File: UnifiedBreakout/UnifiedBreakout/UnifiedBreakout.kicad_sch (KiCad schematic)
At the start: 39 parts, among them J1 24V DC IN, J2 ATX-24, J22 DRAWBAR, J23 MIST, J24 AXIS PWR IN, J25 AXIS PWR OUT, J3 5V BUS, J4 24V BUS, J5 12V BUS, U1 4N35, U7 74HC14

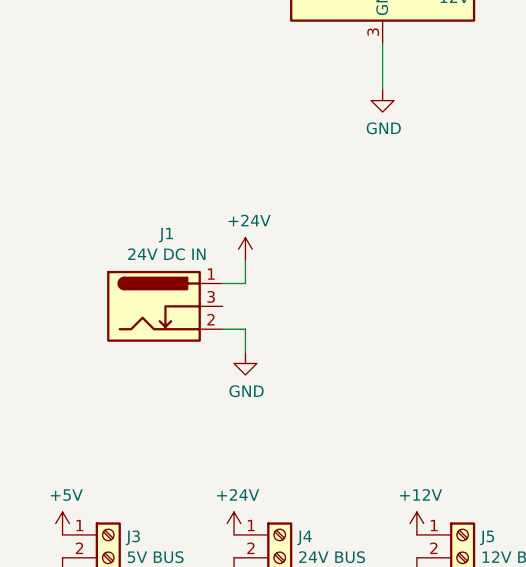
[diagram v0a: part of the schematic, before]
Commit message: Upgrade to new KiCAD version
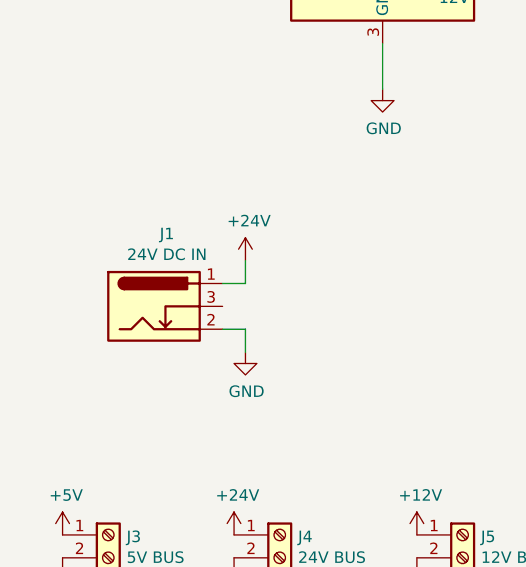
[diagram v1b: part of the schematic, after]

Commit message: WIP updating breakout for electrical enclosure
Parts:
- removed C1, C5: 100n, Capacitor_THT:C_Disc_D5.0mm_W2.5mm_P5.00mm, symbol UnifiedBreakout-rescue:C-Device
- removed C2, C6: 100uF, Capacitor_THT:CP_Radial_D8.0mm_P3.50mm, symbol UnifiedBreakout-rescue:CP-Device
- removed D3: ATX PWR GOOD, LED_THT:LED_D3.0mm, symbol UnifiedBreakout-rescue:LED-Device
- removed D4: ATX STBY, LED_THT:LED_D3.0mm, symbol UnifiedBreakout-rescue:LED-Device
- removed J1: 24V DC IN, SwitchCraft-BarrelJack-RAPC722BK:RAPC722BK, symbol UnifiedBreakout-rescue:Barrel_Jack_Switch-Connector
- removed J2: ATX-24, Connector_Molex:Molex_Mini-Fit_Jr_5569-24A2_2x12_P4.20mm_Horizontal, symbol UnifiedBreakout-rescue:ATX-24-Connector
- removed J22: DRAWBAR, Connector_Phoenix_MSTB:PhoenixContact_MSTBA_2,5_2-G-5,08_1x02_P5.08mm_Horizontal, symbol UnifiedBreakout-rescue:Screw_Terminal_01x02-Connector
- removed J23: MIST, Connector_Phoenix_MSTB:PhoenixContact_MSTBA_2,5_2-G-5,08_1x02_P5.08mm_Horizontal, symbol UnifiedBreakout-rescue:Screw_Terminal_01x02-Connector
- removed J3: 5V BUS, Connector_Phoenix_MSTB:PhoenixContact_MSTBA_2,5_2-G-5,08_1x02_P5.08mm_Horizontal, symbol UnifiedBreakout-rescue:Screw_Terminal_01x02-Connector
- removed J5: 12V BUS, Connector_Phoenix_MSTB:PhoenixContact_MSTBA_2,5_2-G-5,08_1x02_P5.08mm_Horizontal, symbol UnifiedBreakout-rescue:Screw_Terminal_01x02-Connector
- removed R1: 2K2, Resistor_THT:R_Axial_DIN0207_L6.3mm_D2.5mm_P7.62mm_Horizontal, symbol UnifiedBreakout-rescue:R-Device
- removed R25: 10K, Resistor_THT:R_Axial_DIN0207_L6.3mm_D2.5mm_P7.62mm_Horizontal, symbol UnifiedBreakout-rescue:R-Device
- removed R4, R5: 220R, Resistor_THT:R_Axial_DIN0207_L6.3mm_D2.5mm_P7.62mm_Horizontal, symbol UnifiedBreakout-rescue:R-Device
- removed unit 2 of U7
- added J1: DRAWBAR+MIST, Connector_Phoenix_MSTB:PhoenixContact_MSTBA_2,5_2-G-5,08_1x02_P5.08mm_Horizontal, symbol Connector:Screw_Terminal_01x02
- added J2: Screw_Terminal_01x05, Connector_Phoenix_MSTB:PhoenixContact_MSTBA_2,5_5-G-5,08_1x05_P5.08mm_Horizontal, symbol Connector:Screw_Terminal_01x06
- added Q2, Q4: 2N7000, Package_TO_SOT_THT:TO-92_Inline, symbol Transistor_FET:2N7000
- added R1: 10K, Resistor_THT:R_Axial_DIN0207_L6.3mm_D2.5mm_P7.62mm_Horizontal, symbol Device:R
- added unit 6 of U7
- added unit 5 of U7
- added unit 4 of U7
- added unit 2 of U7
- C3, C7: symbol UnifiedBreakout-rescue:C-Device -> Device:C
- C4, C8: symbol UnifiedBreakout-rescue:CP-Device -> Device:C_Polarized
- D1, D2: symbol UnifiedBreakout-rescue:LED-Device -> Device:LED
- H1, H2, H3, H4, H5, H6: symbol UnifiedBreakout-rescue:MountingHole-Mechanical -> Mechanical:MountingHole
- J24, J25: symbol UnifiedBreakout-rescue:Screw_Terminal_01x03-Connector -> Connector:Screw_Terminal_01x03; Farnell PN (none) -> 3041451; MPN 1757255 -> 1729131
- J4: symbol UnifiedBreakout-rescue:Screw_Terminal_01x02-Connector -> Connector:Screw_Terminal_01x02; MPN 1757242 -> (none); Manufacturer Phoenix Contact -> My parts drawers
- R2, R24, R26, R3, R6, R7: symbol UnifiedBreakout-rescue:R-Device -> Device:R
- U1: symbol UnifiedBreakout-rescue:4N35-Isolator -> Isolator:4N35
- U7: symbol UnifiedBreakout-rescue:74HC14-74xx -> 74xx:74HC14
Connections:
- net +5VP: now also R1.1
- net DRAWBAR_VALVE: now also R1.2, U7.3
- net GND: now also Q2.1 (S), Q4.1 (S)
- net MIST RELAY/ENABLE: no longer names the net of U7.6
- net MIST RELAY/ENABLE: now also Q4.2 (G)
- new net: Q2.2 (G), U7.4
- new net: J1.1 (Pin_1), Q2.3 (D)
- new net: J1.2 (Pin_2), Q4.3 (D)
- new net DRAWBAR SW/INPUT: J2.6 (Pin_6)
- new net LIM X/INPUT: J2.1 (Pin_1)
- new net LIM Y/INPUT: J2.2 (Pin_2)
- new net LIM Z/INPUT: J2.3 (Pin_3)
- new net PROBE/INPUT: J2.4 (Pin_4)
- new net TOOL_PROBE/INPUT: J2.5 (Pin_5)
- no-connect marks 0 -> 12
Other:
- removed sheet DRAWBAR RELAY
- removed sheet MIST RELAY
- added sheet TOOL_PROBE (opto_input.kicad_sch)
- sheet ARGON ENCODER ports: added none; removed MESA_5V
- sheet ARGON ESTOP ports: added GND; removed Gnd
- sheet AXIS POWER RELAY ports: added +24V; removed +12V
- sheet DRAWBAR SW ports: added INPUT; removed 24V, 5V
- sheet LIM X ports: added INPUT; removed 24V, 5V
- sheet LIM Y ports: added INPUT; removed 24V, 5V
- sheet LIM Z ports: added INPUT; removed 24V, 5V
- sheet PROBE ports: added INPUT; removed 24V, 5V
- moved on the sheet: R26, U7C

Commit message: Add stacked DA15 part
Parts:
- J2: footprint Connector_Phoenix_MSTB:PhoenixContact_MSTBA_2,5_5-G-5,08_1x05_P5.08mm_Horizontal -> Connector_Phoenix_MSTB:PhoenixContact_MSTBA_2,5_6-G-5,08_1x06_P5.08mm_Horizontal; Farnell PN 3041487 -> 3041499; MPN 1729157 -> 1729160
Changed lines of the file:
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@@
       (effects (font (size 1.27 1.27)) (justify left))
     )
-    (property "Footprint" "Connector_Phoenix_MSTB:PhoenixContact_MSTBA_2,5_5-G-5,08_1x05_P5.08mm_Horizontal" (at 325.12 78.74 0)
+    (property "Footprint" "Connector_Phoenix_MSTB:PhoenixContact_MSTBA_2,5_6-G-5,08_1x06_P5.08mm_Horizontal" (at 325.12 78.74 0)
       (effects (font (size 1.27 1.27)) hide)
     )
@@
       (effects (font (size 1.27 1.27)) hide)
     )
-    (property "Farnell PN" "3041487" (at 325.12 78.74 0)
+    (property "Farnell PN" "3041499" (at 325.12 78.74 0)
       (effects (font (size 1.27 1.27)) hide)
     )
-    (property "MPN" "1729157 " (at 325.12 78.74 0)
+    (property "MPN" "1729160" (at 325.12 78.74 0)
       (effects (font (size 1.27 1.27)) hide)
     )

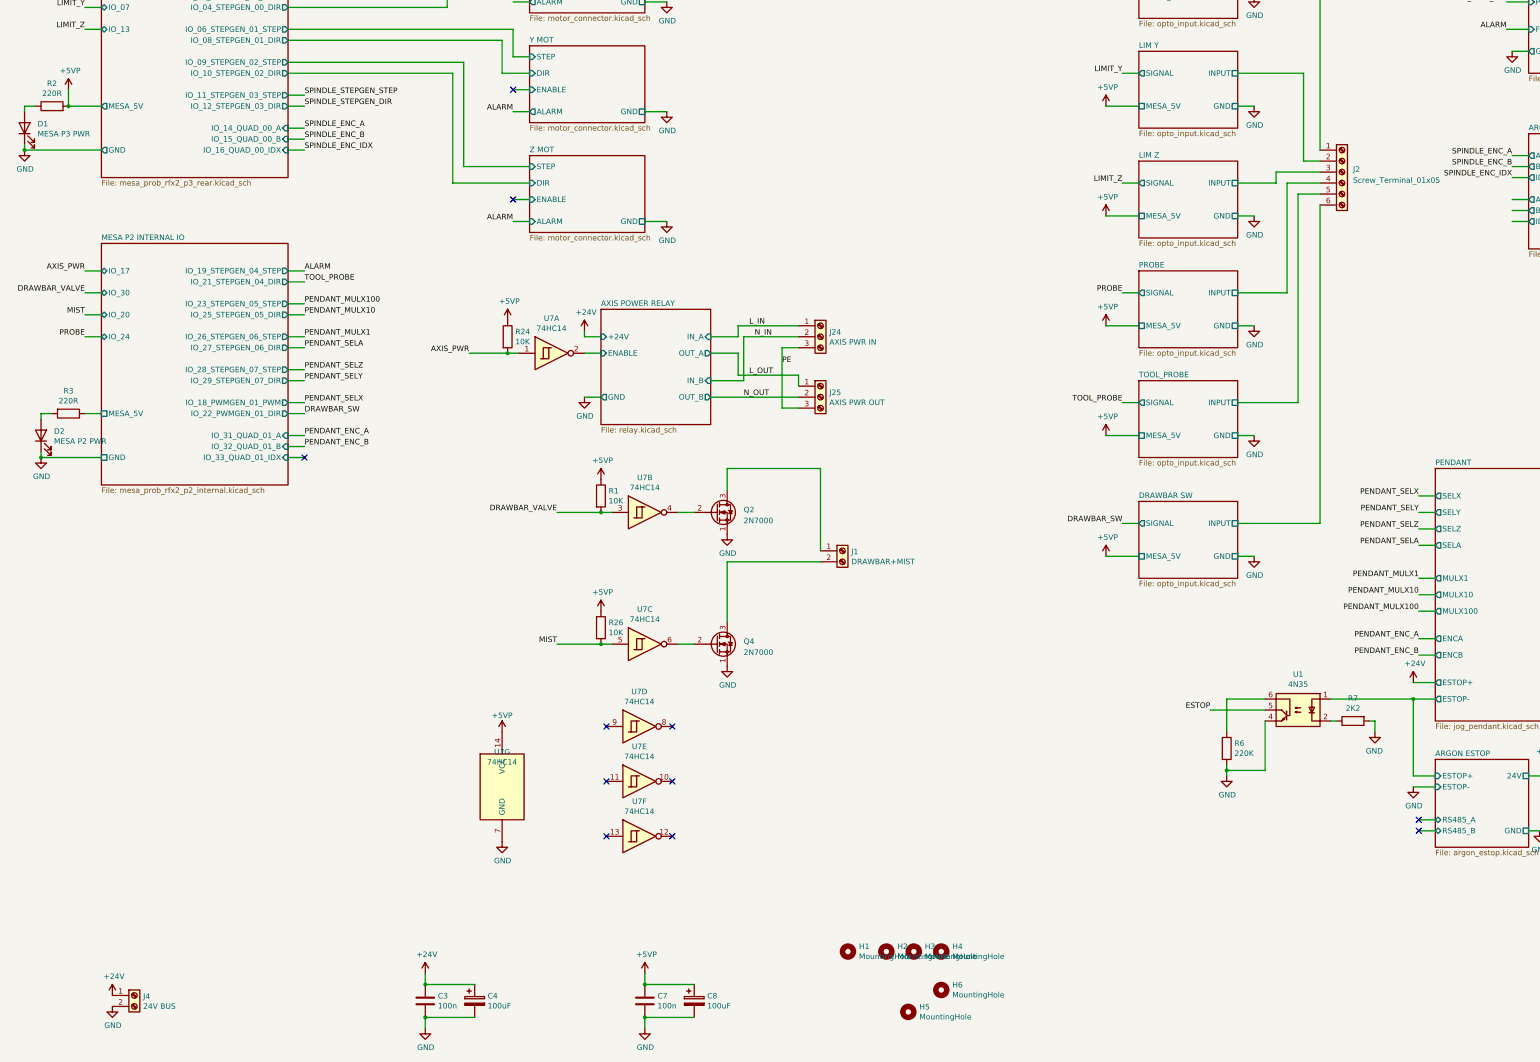
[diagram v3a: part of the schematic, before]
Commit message: Update IO and opto
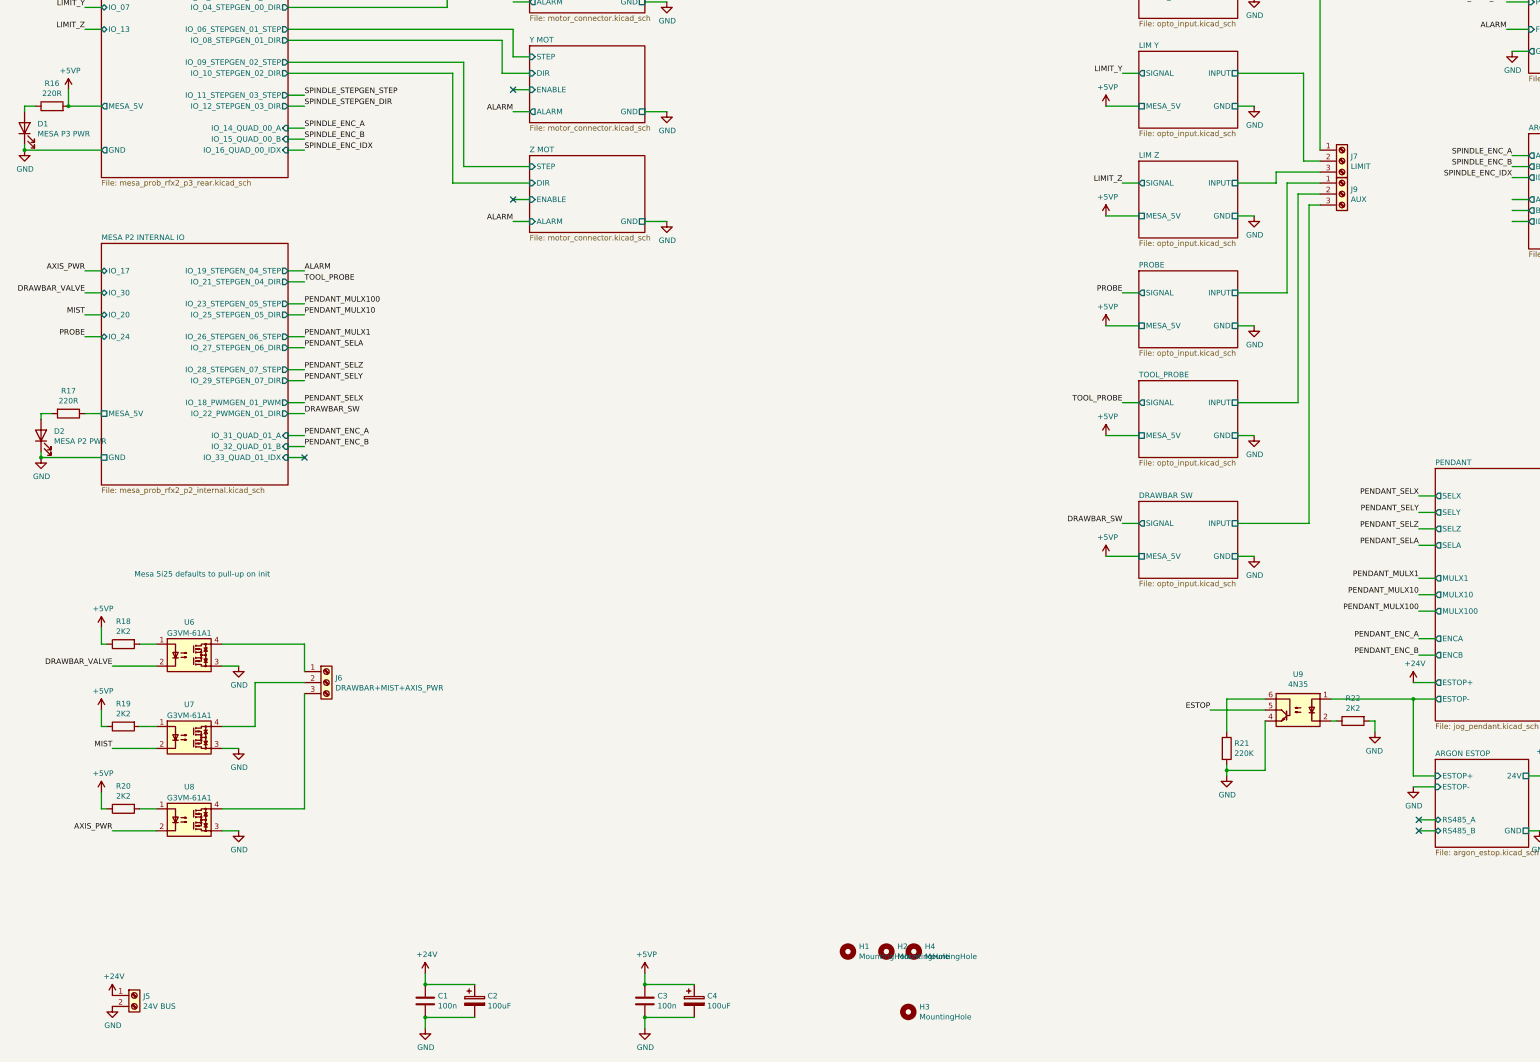
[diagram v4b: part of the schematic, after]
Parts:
- removed H4, H6: MountingHole, MountingHole:MountingHole_3.2mm_M3, symbol Mechanical:MountingHole
- removed J1: DRAWBAR+MIST, Connector_Phoenix_MSTB:PhoenixContact_MSTBA_2,5_2-G-5,08_1x02_P5.08mm_Horizontal, symbol Connector:Screw_Terminal_01x02
- removed J2: Screw_Terminal_01x05, Connector_Phoenix_MSTB:PhoenixContact_MSTBA_2,5_6-G-5,08_1x06_P5.08mm_Horizontal, symbol Connector:Screw_Terminal_01x06
- removed J24: AXIS PWR IN, Connector_Phoenix_MSTB:PhoenixContact_MSTBA_2,5_3-G-5,08_1x03_P5.08mm_Horizontal, symbol Connector:Screw_Terminal_01x03
- removed J25: AXIS PWR OUT, Connector_Phoenix_MSTB:PhoenixContact_MSTBA_2,5_3-G-5,08_1x03_P5.08mm_Horizontal, symbol Connector:Screw_Terminal_01x03
- removed Q2, Q4: 2N7000, Package_TO_SOT_THT:TO-92_Inline, symbol Transistor_FET:2N7000
- removed R1, R24, R26: 10K, Resistor_THT:R_Axial_DIN0207_L6.3mm_D2.5mm_P7.62mm_Horizontal, symbol Device:R
- removed U7: 74HC14, Package_DIP:DIP-14_W7.62mm_LongPads, symbol 74xx:74HC14
- added J6: DRAWBAR+MIST+AXIS_PWR, Connector_Phoenix_MSTB:PhoenixContact_MSTBA_2,5_3-G-5,08_1x03_P5.08mm_Horizontal, symbol Connector:Screw_Terminal_01x03
- added J7: LIMIT, Connector_Phoenix_MSTB:PhoenixContact_MSTBA_2,5_3-G-5,08_1x03_P5.08mm_Horizontal, symbol Connector:Screw_Terminal_01x03
- added J9: AUX, Connector_Phoenix_MSTB:PhoenixContact_MSTBA_2,5_3-G-5,08_1x03_P5.08mm_Horizontal, symbol Connector:Screw_Terminal_01x03
- added R18, R19, R20: 2K2, Resistor_THT:R_Axial_DIN0207_L6.3mm_D2.5mm_P7.62mm_Horizontal, symbol Device:R
- added U6, U7, U8: G3VM-61A1, Package_DIP:DIP-4_W7.62mm, symbol Relay_SolidState:TLP222A
- J5: renamed from J4; Farnell PN (none) -> 3705171; MPN (none) -> 1757242; Manufacturer My parts drawers -> PHOENIX CONTACT
- renumbered C3 to C1, C4 to C2, C7 to C3, C8 to C4, H5 to H3, H3 to H4, R2 to R16, R3 to R17, R6 to R21, R7 to R22, U1 to U9
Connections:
- net +5VP: now also R18.1, R19.1, R20.1
- net AXIS_PWR: now also U8.2
- net DRAWBAR SW/INPUT: now also J9.3 (Pin_3)
- net DRAWBAR_VALVE: now also U6.2
- net GND: now also U6.3, U7.3, U8.3
- net LIM X/INPUT: now also J7.1 (Pin_1)
- net LIM Y/INPUT: now also J7.2 (Pin_2)
- net LIM Z/INPUT: now also J7.3 (Pin_3)
- net MIST: now also U7.2
- net PROBE/INPUT: now also J9.1 (Pin_1)
- net TOOL_PROBE/INPUT: now also J9.2 (Pin_2)
- new net: J6.1 (Pin_1), U6.4
- new net: J6.2 (Pin_2), U7.4
- new net: J6.3 (Pin_3), U8.4
- new net: R18.2, U6.1
- new net: R19.2, U7.1
- new net: R20.2, U8.1
- no-connect marks 12 -> 6
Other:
- removed sheet AXIS POWER RELAY
- note added: "Mesa 5i25 defaults to pull-up on init"

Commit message: Tweaks and stuff
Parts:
- added D3: +24V, LED_THT:LED_D3.0mm, symbol Device:LED
- added R2: 220R, Resistor_THT:R_Axial_DIN0207_L6.3mm_D2.5mm_P7.62mm_Horizontal, symbol Device:R
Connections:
- net +24V: now also R2.1
- net GND: now also D3.1 (K)
- new net: D3.2 (A), R2.2
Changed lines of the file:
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@@
+    (stroke (width 0) (type solid))
+  )
+  (wire (pts (xy 69.85 260.35) (xy 69.85 261.62))
     (stroke (width 0) (type solid))
   )
@@
     (stroke (width 0) (type solid))
   )
+  (wire (pts (xy 80.01 256.54) (xy 80.01 260.35))
+    (stroke (width 0) (type solid))
+  )
   (wire (pts (xy 38.1 30.48) (xy 34.29 30.48))
     (stroke (width 0) (type solid))
@@
     (stroke (width 0) (type solid))
   )
+  (wire (pts (xy 72.39 260.35) (xy 69.85 260.35))
+    (stroke (width 0) (type solid))
+  )
   (wire (pts (xy 30.48 63.5) (xy 38.1 63.5))
     (stroke (width 0) (type solid))
@@
   )
   (wire (pts (xy 81.28 63.5) (xy 85.09 63.5))
+    (stroke (width 0) (type solid))
+  )
+  (wire (pts (xy 69.85 269.24) (xy 69.85 270.51))
     (stroke (width 0) (type solid))
   )
@@
     )
   )
+  (symbol (lib_id "Device:LED") (at 69.85 265.43 90) (unit 1)
+    (in_bom yes) (on_board yes) (dnp no)
+    (property "Reference" "D3" (at 72.8472 264.4394 90)
+      (effects (font (size 1.27 1.27)) (justify right))
+    )
+    (property "Value" "+24V" (at 72.8472 266.7508 90)
+      (effects (font (size 1.27 1.27)) (justify right))
+    )
+    (property "Footprint" "LED_THT:LED_D3.0mm" (at 69.85 265.43 0)
+      (effects (font (size 1.27 1.27)) hide)
+    )
+    (property "Datasheet" "~" (at 69.85 265.43 0)
+      (effects (font (size 1.27 1.27)) hide)
+    )
+    (property "Farnell PN" "" (at 69.85 265.43 0)
+      (effects (font (size 1.27 1.27)) hide)
+    )
+    (pin "1")
+    (pin "2")
+    (instances
+      (project "UnifiedBreakout"
+        (path "/e63e39d7-6ac0-4ffd-8aa3-1841a4541b55"
+          (reference "D3") (unit 1)
+        )
+      )
+    )
+  )
   (symbol (lib_id "Device:R") (at 43.18 207.01 90) (mirror x) (unit 1)
     (in_bom yes) (on_board yes) (dnp no)
@@
     )
   )
+  (symbol (lib_id "power:GND") (at 69.85 270.51 0) (unit 1)
+    (in_bom yes) (on_board yes) (dnp no)
+    (property "Reference" "#PWR041" (at 69.85 276.86 0)
+      (effects (font (size 1.27 1.27)) hide)
+    )
+    (property "Value" "GND" (at 69.977 274.9042 0)
+      (effects (font (size 1.27 1.27)))
+    )
+    (property "Footprint" "" (at 69.85 270.51 0)
+      (effects (font (size 1.27 1.27)) hide)
+    )
+    (property "Datasheet" "" (at 69.85 270.51 0)
+      (effects (font (size 1.27 1.27)) hide)
+    )
+    (pin "1")
+    (instances
+      (project "UnifiedBreakout"
+        (path "/e63e39d7-6ac0-4ffd-8aa3-1841a4541b55"
+          (reference "#PWR041") (unit 1)
+        )
+      )
+    )
+  )
   (symbol (lib_id "Device:R") (at 43.18 226.06 90) (mirror x) (unit 1)
     (in_bom yes) (on_board yes) (dnp no)
@@
         )
       )
+    )
+  )
+  (symbol (lib_id "Device:R") (at 76.2 260.35 270) (unit 1)
+    (in_bom yes) (on_board yes) (dnp no)
+    (property "Reference" "R2" (at 76.2 255.0922 90)
+      (effects (font (size 1.27 1.27)))
+    )
+    (property "Value" "220R" (at 76.2 257.4036 90)
+      (effects (font (size 1.27 1.27)))
+    )
+    (property "Footprint" "Resistor_THT:R_Axial_DIN0207_L6.3mm_D2.5mm_P7.62mm_Horizontal" (at 76.2 258.572 90)
+      (effects (font (size 1.27 1.27)) hide)
+    )
+    (property "Datasheet" "~" (at 76.2 260.35 0)
+      (effects (font (size 1.27 1.27)) hide)
+    )
+    (property "MPN" "CFR-25JB-52-220R" (at 76.2 260.35 0)
+      (effects (font (size 1.27 1.27)) hide)
+    )
+    (property "Manufacturer" "Yageo" (at 76.2 260.35 0)
+      (effects (font (size 1.27 1.27)) hide)
+    )
+    (property "Farnell PN" "" (at 76.2 260.35 0)
+      (effects (font (size 1.27 1.27)) hide)
+    )
+    (pin "1")
+    (pin "2")
+    (instances
+      (project "UnifiedBreakout"
+        (path "/e63e39d7-6ac0-4ffd-8aa3-1841a4541b55"
+          (reference "R2") (unit 1)
+        )
+      )
+    )
+  )
+  (symbol (lib_id "power:+24V") (at 80.01 256.54 0) (unit 1)
+    (in_bom yes) (on_board yes) (dnp no)
+    (property "Reference" "#PWR042" (at 80.01 260.35 0)
+      (effects (font (size 1.27 1.27)) hide)
+    )
+    (property "Value" "+24V" (at 80.391 252.1458 0)
+      (effects (font (size 1.27 1.27)))
+    )
+    (property "Footprint" "" (at 80.01 256.54 0)
+      (effects (font (size 1.27 1.27)) hide)
+    )
+    (property "Datasheet" "" (at 80.01 256.54 0)
+      (effects (font (size 1.27 1.27)) hide)
+    )
+    (pin "1")
+    (instances
+      (project "UnifiedBreakout"
+        (path "/e63e39d7-6ac0-4ffd-8aa3-1841a4541b55"
+          (reference "#PWR042") (unit 1)
+        )
+      )

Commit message: Started some layout
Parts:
- added H5, H6: MountingHole, MountingHole:MountingHole_3.2mm_M3, symbol Mechanical:MountingHole
- D1, D2: Farnell PN (none) -> 1581114; MPN (none) -> MCL034GD; Manufacturer (none) -> MULTICOMP PRO
- D3: Farnell PN (none) -> 1581122; MPN (none) -> MCL034MT; Manufacturer (none) -> MULTICOMP PRO

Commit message: Some layout
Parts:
- H1, H2, H3, H4, H5, H6: footprint MountingHole:MountingHole_3.2mm_M3 -> MountingHole:MountingHole_3.2mm_M3_Pad; symbol Mechanical:MountingHole -> Mechanical:MountingHole_Pad
- renumbered J5 to J6, J6 to J7, J7 to J8, R16 to R11, R17 to R12, R18 to R13, R19 to R14, R20 to R15, R2 to R16, R21 to R17, R22 to R18, U6 to U4, U7 to U5, U8 to U6, U9 to U7
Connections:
- net MESA_P3_5V: now reaches D2.2 (A), R12.2
- no-connect marks 6 -> 12
